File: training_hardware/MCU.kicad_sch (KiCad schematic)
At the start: 2 parts, among them J1 RJ45_LED_Shielded, U1 Teensy4.1_DEV-16771

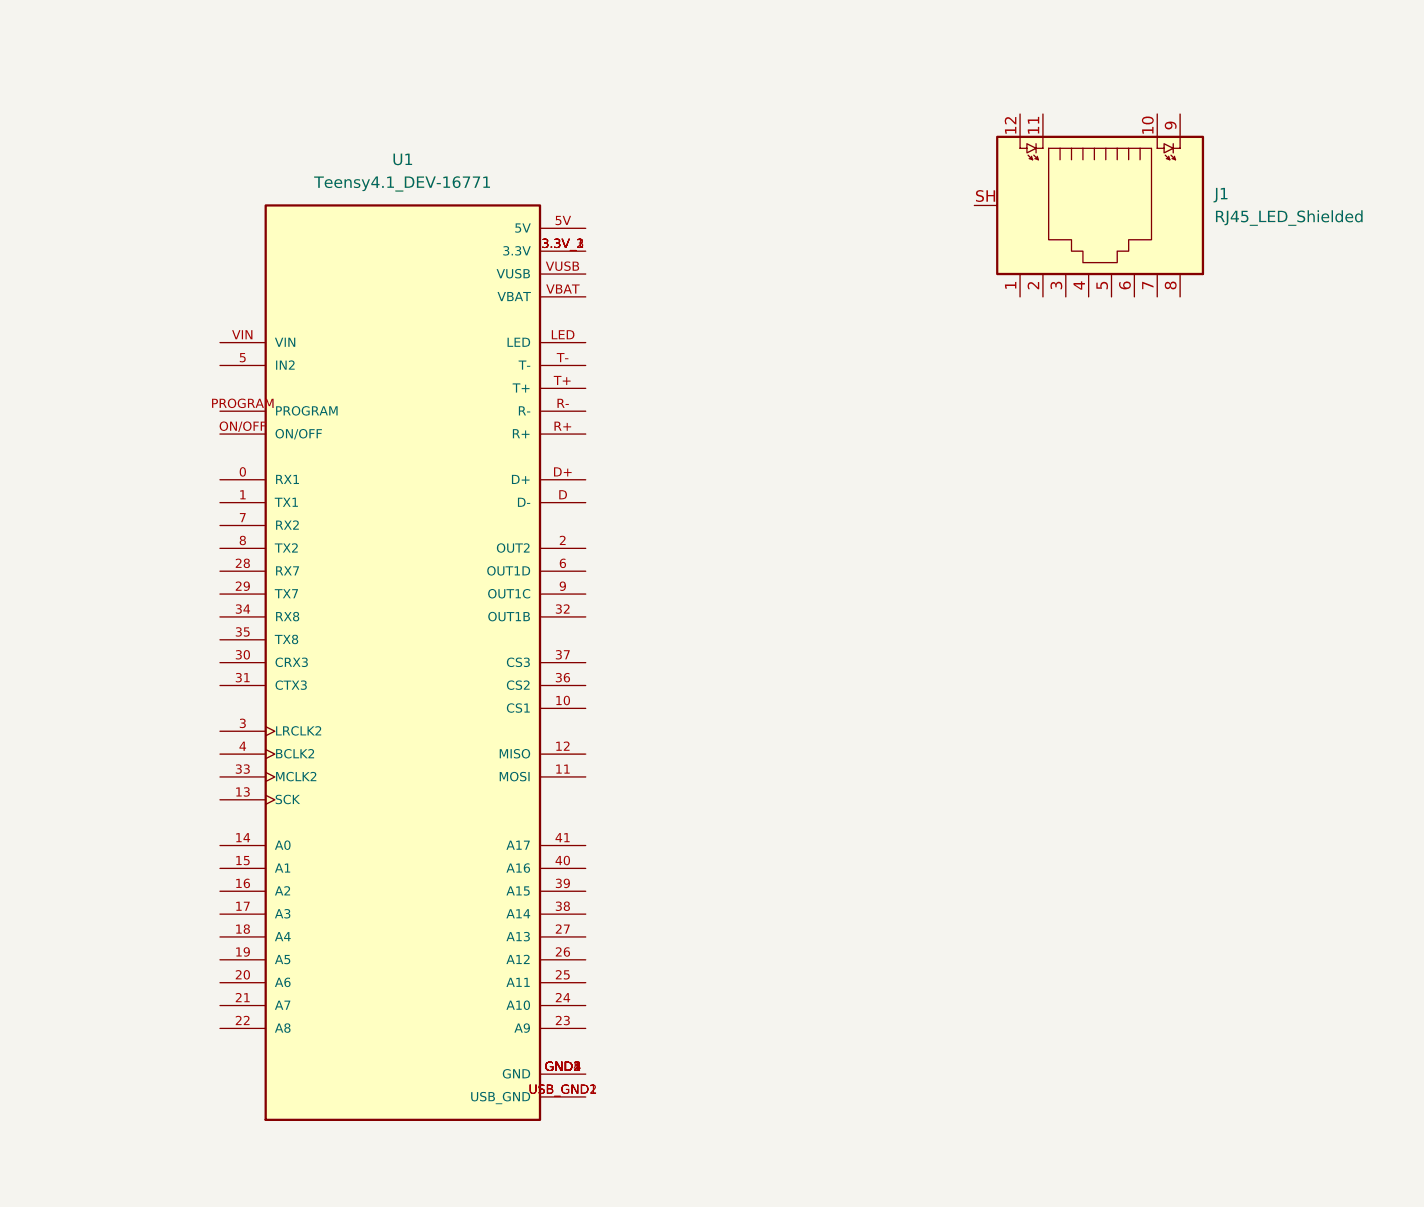
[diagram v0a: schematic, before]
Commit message: Add Ethernet
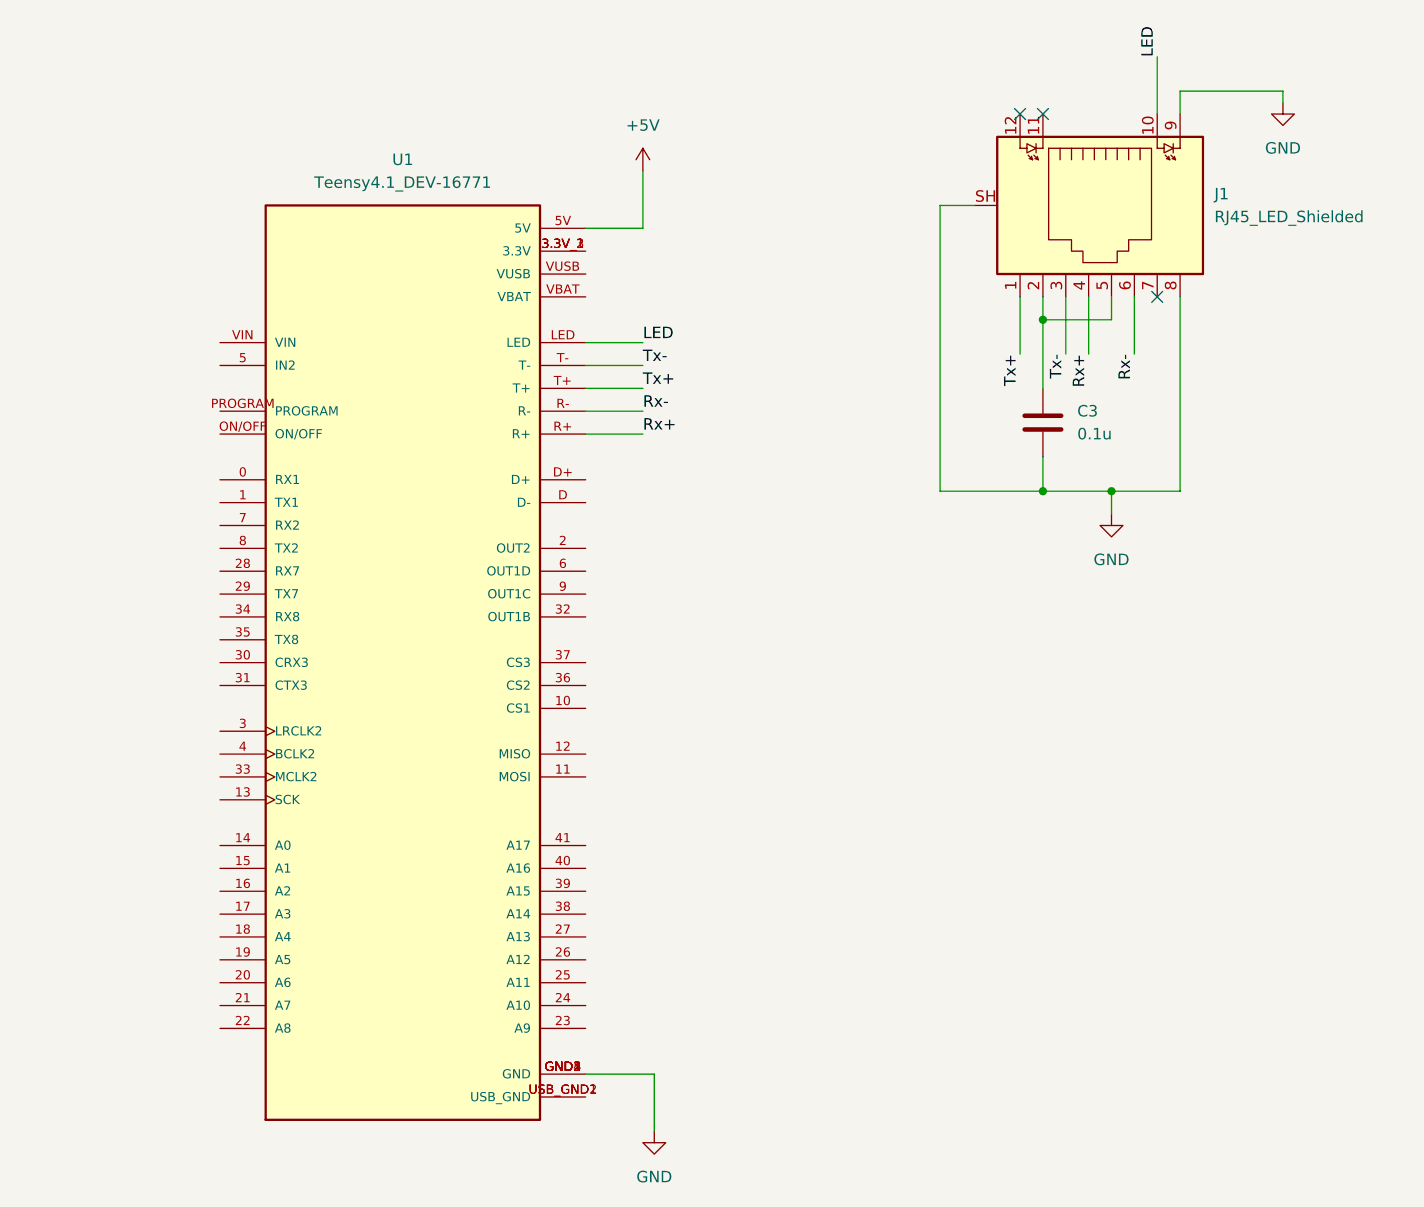
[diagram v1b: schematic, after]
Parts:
- added C3: 0.1u, symbol Device:C
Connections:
- net Tx+: now reaches J1.1
- net Tx+: now also U1.T+
- net LED: now reaches J1.10
- net LED: now also U1.LED
- net at J1.2: now also J1.5, C3.1
- net Tx-: now reaches J1.3
- net Tx-: now also U1.T-
- net Rx+: now reaches J1.4
- net Rx+: now also U1.R+
- net Rx-: now reaches J1.6
- net Rx-: now also U1.R-
- net GND: now reaches J1.8
- net GND: now also J1.9, J1.SH, U1.GND1 (GND), U1.GND2 (GND), U1.GND3 (GND), U1.GND4 (GND), U1.GND5 (GND), C3.2
- net +5V: now reaches U1.5V
- no-connect marks 0 -> 3

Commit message: Finnish Schematic
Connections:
- net STBY: now reaches U1.2 (OUT2)
- net CTX1: now reaches U1.22 (A8)
- net CRX1: now reaches U1.23 (A9)
- net +3V3: now reaches U1.3.3V_1 (3.3V), U1.3.3V_2 (3.3V), U1.3.3V_3 (3.3V)
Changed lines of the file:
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@@
+	(wire
+		(pts
+			(xy 107.95 142.24) (xy 123.19 142.24)
+		)
+		(stroke
+			(width 0)
+			(type default)
+		)
+	)
 	(wire
 		(pts
@@
 	(wire
 		(pts
+			(xy 163.83 142.24) (xy 171.45 142.24)
+		)
+		(stroke
+			(width 0)
+			(type default)
+		)
+	)
+	(wire
+		(pts
 			(xy 163.83 53.34) (xy 170.18 53.34)
 		)
@@
 	(wire
 		(pts
+			(xy 176.53 46.99) (xy 176.53 55.88)
+		)
+		(stroke
+			(width 0)
+			(type default)
+		)
+	)
+	(wire
+		(pts
 			(xy 170.18 46.99) (xy 170.18 53.34)
 		)
@@
 	(wire
 		(pts
+			(xy 163.83 55.88) (xy 176.53 55.88)
+		)
+		(stroke
+			(width 0)
+			(type default)
+		)
+	)
+	(wire
+		(pts
 			(xy 222.25 82.55) (xy 222.25 85.09)
 		)
@@
 		(pts
 			(xy 229.87 38.1) (xy 241.3 38.1)
+		)
+		(stroke
+			(width 0)
+			(type default)
+		)
+	)
+	(wire
+		(pts
+			(xy 163.83 88.9) (xy 171.45 88.9)
 		)
 		(stroke
@@
 			)
 			(justify left bottom)
+		)
+	)
+	(hierarchical_label "CTX1"
+		(shape output)
+		(at 107.95 142.24 180)
+		(effects
+			(font
+				(size 1.27 1.27)
+			)
+			(justify right)
+		)
+	)
+	(hierarchical_label "STBY"
+		(shape output)
+		(at 171.45 88.9 0)
+		(effects
+			(font
+				(size 1.27 1.27)
+			)
+			(justify left)
+		)
+	)
+	(hierarchical_label "CRX1"
+		(shape input)
+		(at 171.45 142.24 0)
+		(effects
+			(font
+				(size 1.27 1.27)
+			)
+			(justify left)
 		)
 	)
@@
 					(unit 1)
 				)
+			)
+		)
+	)
+	(symbol
+		(lib_id "power:+3V3")
+		(at 176.53 46.99 0)
+		(unit 1)
+		(exclude_from_sim no)
+		(in_bom yes)
+		(on_board yes)
+		(dnp no)
+		(fields_autoplaced yes)
+		(property "Reference" "#PWR016"
+			(at 176.53 50.8 0)
+			(effects
+				(font
+					(size 1.27 1.27)
+				)
+				(hide yes)
+			)
+		)
+		(property "Value" "+3V3"
+			(at 176.53 41.91 0)
+			(effects
+				(font
+					(size 1.27 1.27)
+				)
+			)
+		)
+		(property "Footprint" ""
+			(at 176.53 46.99 0)
+			(effects
+				(font
+					(size 1.27 1.27)
+				)
+				(hide yes)
+			)
+		)
+		(property "Datasheet" ""
+			(at 176.53 46.99 0)
+			(effects
+				(font
+					(size 1.27 1.27)
+				)
+				(hide yes)
+			)
+		)
+		(property "Description" "Power symbol creates a global label with name \"+3V3\""
+			(at 176.53 46.99 0)
+			(effects
+				(font
+					(size 1.27 1.27)
+				)
+				(hide yes)
+			)
+		)
+		(pin "1"
+		)
+		(instances
+			(project ""
+				(path "/19aa0e78-5ab4-46df-84c9-9ca161187559/7e06b3c1-2423-42b6-bbd6-08ed46d7df02"
+					(reference "#PWR016")
+					(unit 1)
+				)
